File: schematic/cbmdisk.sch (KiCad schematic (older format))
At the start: 26 parts, among them IC1 74HC4050, IC2 ATMEGA1284-P, K1 CONN_3, P1 CONN_2, P2 CONN_12, P3 CONN_12, P4 CONN_5X2, P5 CONN_9, P6 CONN_4, P7 CONN_6, SW1 SW_PUSH, SW2 SWITCH_INV, U1 LM1085, U2 7805, X1 20 MHz

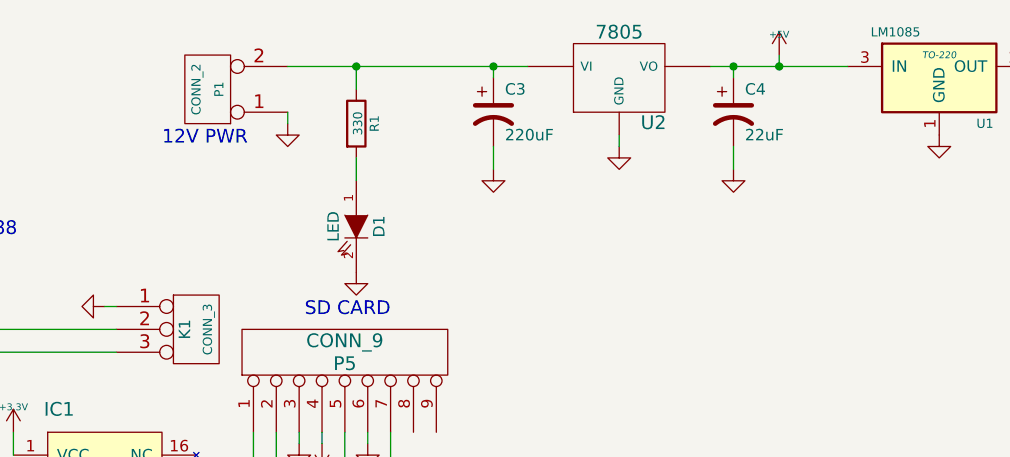
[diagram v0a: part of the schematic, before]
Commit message: remove 5V regulator (use 5V switching power supply)
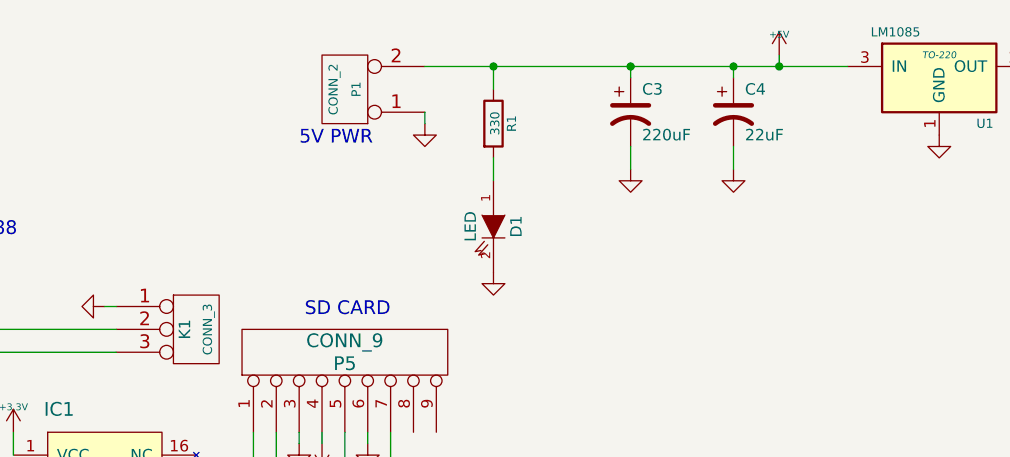
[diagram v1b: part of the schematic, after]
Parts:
- removed U2: 7805, ~, symbol 7805
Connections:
- wire segments 141 -> 139
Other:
- note added: "5V PWR"
- note removed: "12V PWR"
- moved on the sheet: C3, D1, P1, R1
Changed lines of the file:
@@
-$EndComp
-$Comp
-L 7805 U2
-U 1 1 55AB66E8
-P 8400 750
-F 0 "U2" H 8550 554 60  0000 C CNN
-F 1 "7805" H 8400 950 60  0000 C CNN
-F 2 "~" H 8400 750 60  0000 C CNN
-F 3 "~" H 8400 750 60  0000 C CNN
-	1    8400 750
-	1    0    0    -1
 $EndComp
 $Comp
 L CONN_2 P1
 U 1 1 55AB6701
-P 6600 800
-F 0 "P1" V 6550 800 40  0000 C CNN
-F 1 "CONN_2" V 6650 800 40  0000 C CNN
-F 2 "~" H 6600 800 60  0000 C CNN
-F 3 "~" H 6600 800 60  0000 C CNN
-	1    6600 800
+P 7200 800
+F 0 "P1" V 7150 800 40  0000 C CNN
+F 1 "CONN_2" V 7250 800 40  0000 C CNN
+F 2 "~" H 7200 800 60  0000 C CNN
+F 3 "~" H 7200 800 60  0000 C CNN
+	1    7200 800
 	-1   0    0    1
 $EndComp
@@
 L GND #PWR5
 U 1 1 55AB671A
-P 6950 950
-F 0 "#PWR5" H 6950 950 30  0001 C CNN
-F 1 "GND" H 6950 880 30  0001 C CNN
-F 2 "" H 6950 950 60  0000 C CNN
-F 3 "" H 6950 950 60  0000 C CNN
-	1    6950 950
-	1    0    0    -1
-$EndComp
-Text Notes 6400 1050 0    60   ~ 0
-12V PWR
+P 7550 950
+F 0 "#PWR5" H 7550 950 30  0001 C CNN
+F 1 "GND" H 7550 880 30  0001 C CNN
+F 2 "" H 7550 950 60  0000 C CNN
+F 3 "" H 7550 950 60  0000 C CNN
+	1    7550 950
+	1    0    0    -1
+$EndComp
+Text Notes 7000 1050 0    60   ~ 0
+5V PWR
 $Comp
 L CP1 C3
 U 1 1 55AB68A1
-P 7850 900
-F 0 "C3" H 7900 1000 50  0000 L CNN
-F 1 "220uF" H 7900 800 50  0000 L CNN
-F 2 "~" H 7850 900 60  0000 C CNN
-F 3 "~" H 7850 900 60  0000 C CNN
-	1    7850 900
+P 8450 900
+F 0 "C3" H 8500 1000 50  0000 L CNN
+F 1 "220uF" H 8500 800 50  0000 L CNN
+F 2 "~" H 8450 900 60  0000 C CNN
+F 3 "~" H 8450 900 60  0000 C CNN
+	1    8450 900
 	1    0    0    -1
 $EndComp
@@
 L GND #PWR10
 U 1 1 55AB68B0
-P 7850 1150
-F 0 "#PWR10" H 7850 1150 30  0001 C CNN
-F 1 "GND" H 7850 1080 30  0001 C CNN
-F 2 "" H 7850 1150 60  0000 C CNN
-F 3 "" H 7850 1150 60  0000 C CNN
-	1    7850 1150
+P 8450 1150
+F 0 "#PWR10" H 8450 1150 30  0001 C CNN
+F 1 "GND" H 8450 1080 30  0001 C CNN
+F 2 "" H 8450 1150 60  0000 C CNN
+F 3 "" H 8450 1150 60  0000 C CNN
+	1    8450 1150
 	1    0    0    -1
 $EndComp
@@
 $EndComp
 $Comp
-L GND #PWR8
-U 1 1 55AB6C63
-P 8400 1050
-F 0 "#PWR8" H 8400 1050 30  0001 C CNN
-F 1 "GND" H 8400 980 30  0001 C CNN
-F 2 "" H 8400 1050 60  0000 C CNN
-F 3 "" H 8400 1050 60  0000 C CNN
-	1    8400 1050
-	1    0    0    -1
-$EndComp
-$Comp
 L LED D1
 U 1 1 55AB6CED
-P 7250 1400
-F 0 "D1" H 7250 1500 50  0000 C CNN
-F 1 "LED" H 7250 1300 50  0000 C CNN
-F 2 "~" H 7250 1400 60  0000 C CNN
-F 3 "~" H 7250 1400 60  0000 C CNN
-	1    7250 1400
+P 7850 1400
+F 0 "D1" H 7850 1500 50  0000 C CNN
+F 1 "LED" H 7850 1300 50  0000 C CNN
+F 2 "~" H 7850 1400 60  0000 C CNN
+F 3 "~" H 7850 1400 60  0000 C CNN
+	1    7850 1400
 	0    1    1    0
 $EndComp
@@
 L R R1
 U 1 1 55AB6CFC
-P 7250 950
-F 0 "R1" V 7330 950 40  0000 C CNN
-F 1 "330" V 7257 951 40  0000 C CNN
-F 2 "~" V 7180 950 30  0000 C CNN
-F 3 "~" H 7250 950 30  0000 C CNN
-	1    7250 950
+P 7850 950
+F 0 "R1" V 7930 950 40  0000 C CNN
+F 1 "330" V 7857 951 40  0000 C CNN
+F 2 "~" V 7780 950 30  0000 C CNN
+F 3 "~" H 7850 950 30  0000 C CNN
+	1    7850 950
 	1    0    0    -1
 $EndComp
@@
 L GND #PWR15
 U 1 1 55AB6D15
-P 7250 1600
-F 0 "#PWR15" H 7250 1600 30  0001 C CNN
-F 1 "GND" H 7250 1530 30  0001 C CNN
-F 2 "" H 7250 1600 60  0000 C CNN
-F 3 "" H 7250 1600 60  0000 C CNN
-	1    7250 1600
+P 7850 1600
+F 0 "#PWR15" H 7850 1600 30  0001 C CNN
+F 1 "GND" H 7850 1530 30  0001 C CNN
+F 2 "" H 7850 1600 60  0000 C CNN
+F 3 "" H 7850 1600 60  0000 C CNN
+	1    7850 1600
 	1    0    0    -1
 $EndComp
@@
 	5700 4600 5750 4600
 Wire Wire Line
-	6950 950  6950 900
-Wire Wire Line
-	6950 700  8000 700
-Wire Wire Line
-	7850 1050 7850 1150
+	7550 950  7550 900
+Wire Wire Line
+	8450 1050 8450 1150
 Wire Wire Line
 	8900 1050 8900 1150
-Wire Wire Line
-	8800 700  9400 700
-Wire Wire Line
-	8400 1050 8400 1000
 Wire Wire Line
 	3850 4500 3650 4500
@@
 RESET
 Wire Wire Line
-	7250 700  7250 800
-Connection ~ 7250 700
-Wire Wire Line
-	7250 1100 7250 1200
+	7850 700  7850 800
+Connection ~ 7850 700
+Wire Wire Line
+	7850 1100 7850 1200
 Wire Wire Line
 	8900 700  8900 750
 Connection ~ 8900 700
 Wire Wire Line
-	7850 700  7850 750
-Connection ~ 7850 700
+	8450 700  8450 750
+Connection ~ 8450 700
 Wire Wire Line
 	10350 1050 10350 1100
@@
 Wire Wire Line
 	2050 1200 2050 1250
+Wire Wire Line
+	9400 700  7550 700
 $EndSCHEMATC

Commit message: big cleanup, remove network parts
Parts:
- removed P4: CONN_5X2, ~, symbol CONN_5X2
- removed P7: CONN_6, ~, symbol CONN_6
- removed SW2: SWITCH_INV, ~, symbol SWITCH_INV
- added J?: CONN_02X04, symbol CONN_02X04
- D1, D2: symbol LED -> LED-RESCUE-cbmdisk
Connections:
- net labels removed: CLKOUT, CS, ETH_INT, IEC_ATN, IEC_CLK, IEC_DATA, IEC_RESET, IEC_SRQ, SI, SO, VCC, bRESET
- wire segments 139 -> 106
- no-connect marks 0 -> 13
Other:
- note added: "DEBUG"
- note removed: "ETH Module"
- note removed: "IEC PORT"
- note removed: "IEEE488 / IEC"
- moved on the sheet: C2, C3, C4, D1, P1, P5, R1, U1

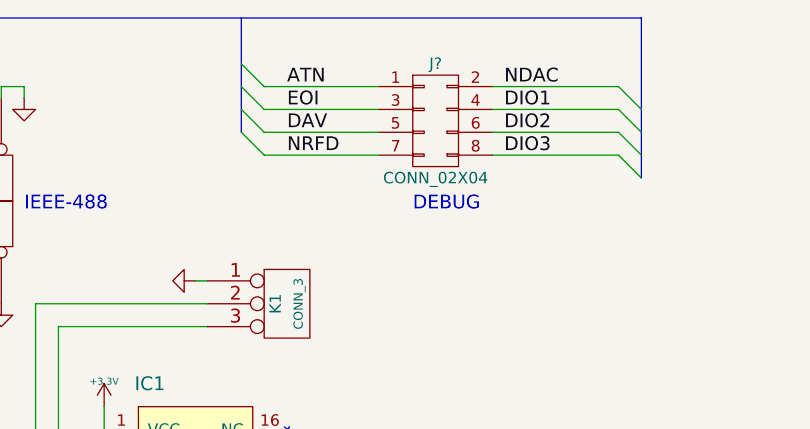
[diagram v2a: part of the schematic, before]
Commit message: update schematic
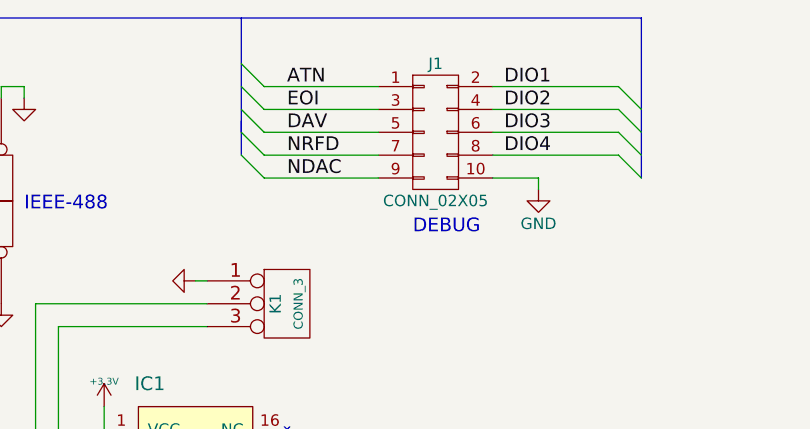
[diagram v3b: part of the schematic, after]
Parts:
- removed J?: CONN_02X04, symbol CONN_02X04
- added J1: CONN_02X05, symbol CONN_02X05
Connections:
- net ATN: now also J1.1 (P1)
- net DAV: now also J1.5 (P5)
- net DIO1: now also J1.2 (P2)
- net DIO2: now also J1.4 (P4)
- net DIO3: now also J1.6 (P6)
- net DIO4: now also J1.8 (P8)
- net EOI: now also J1.3 (P3)
- net GND: now also J1.10 (P10)
- net NDAC: now also J1.9 (P9)
- net NRFD: now also J1.7 (P7)
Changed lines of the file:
@@
 $EndComp
 $Comp
-L GND #PWR24
+L GND #PWR15
 U 1 1 546E9A2F
 P 650 1900
-F 0 "#PWR24" H 650 1900 30  0001 C CNN
+F 0 "#PWR15" H 650 1900 30  0001 C CNN
 F 1 "GND" H 650 1830 30  0001 C CNN
 F 2 "" H 650 1900 60  0000 C CNN
@@
 $EndComp
 $Comp
-L GND #PWR29
+L GND #PWR17
 U 1 1 546E9A3E
 P 650 2500
-F 0 "#PWR29" H 650 2500 30  0001 C CNN
+F 0 "#PWR17" H 650 2500 30  0001 C CNN
 F 1 "GND" H 650 2430 30  0001 C CNN
 F 2 "" H 650 2500 60  0000 C CNN
@@
 $EndComp
 $Comp
-L GND #PWR40
+L GND #PWR28
 U 1 1 5470B949
 P 2650 5300
-F 0 "#PWR40" H 2650 5300 30  0001 C CNN
+F 0 "#PWR28" H 2650 5300 30  0001 C CNN
 F 1 "GND" H 2650 5230 30  0001 C CNN
 F 2 "" H 2650 5300 60  0000 C CNN
@@
 $EndComp
 $Comp
-L GND #PWR39
+L GND #PWR27
 U 1 1 5470B958
 P 2450 5300
-F 0 "#PWR39" H 2450 5300 30  0001 C CNN
+F 0 "#PWR27" H 2450 5300 30  0001 C CNN
 F 1 "GND" H 2450 5230 30  0001 C CNN
 F 2 "" H 2450 5300 60  0000 C CNN
@@
 $EndComp
 $Comp
-L GND #PWR4
+L GND #PWR2
 U 1 1 5470F400
 P 5400 950
-F 0 "#PWR4" H 5400 950 30  0001 C CNN
+F 0 "#PWR2" H 5400 950 30  0001 C CNN
 F 1 "GND" H 5400 880 30  0001 C CNN
 F 2 "" H 5400 950 60  0000 C CNN
@@
 $EndComp
 $Comp
-L GND #PWR17
+L GND #PWR8
 U 1 1 5470F40F
 P 4700 1850
-F 0 "#PWR17" H 4700 1850 30  0001 C CNN
+F 0 "#PWR8" H 4700 1850 30  0001 C CNN
 F 1 "GND" H 4700 1780 30  0001 C CNN
 F 2 "" H 4700 1850 60  0000 C CNN
@@
 $EndComp
 $Comp
-L GND #PWR18
+L GND #PWR9
 U 1 1 5470F41E
 P 4800 1850
-F 0 "#PWR18" H 4800 1850 30  0001 C CNN
+F 0 "#PWR9" H 4800 1850 30  0001 C CNN
 F 1 "GND" H 4800 1780 30  0001 C CNN
 F 2 "" H 4800 1850 60  0000 C CNN
@@
 $EndComp
 $Comp
-L GND #PWR19
+L GND #PWR10
 U 1 1 5470F42D
 P 4900 1850
-F 0 "#PWR19" H 4900 1850 30  0001 C CNN
+F 0 "#PWR10" H 4900 1850 30  0001 C CNN
 F 1 "GND" H 4900 1780 30  0001 C CNN
 F 2 "" H 4900 1850 60  0000 C CNN
@@
 $EndComp
 $Comp
-L GND #PWR20
+L GND #PWR11
 U 1 1 5470F43C
 P 5000 1850
-F 0 "#PWR20" H 5000 1850 30  0001 C CNN
+F 0 "#PWR11" H 5000 1850 30  0001 C CNN
 F 1 "GND" H 5000 1780 30  0001 C CNN
 F 2 "" H 5000 1850 60  0000 C CNN
@@
 $EndComp
 $Comp
-L GND #PWR21
+L GND #PWR12
 U 1 1 5470F44B
 P 5100 1850
-F 0 "#PWR21" H 5100 1850 30  0001 C CNN
+F 0 "#PWR12" H 5100 1850 30  0001 C CNN
 F 1 "GND" H 5100 1780 30  0001 C CNN
 F 2 "" H 5100 1850 60  0000 C CNN
@@
 $EndComp
 $Comp
-L GND #PWR22
+L GND #PWR13
 U 1 1 5470F45A
 P 5200 1850
-F 0 "#PWR22" H 5200 1850 30  0001 C CNN
+F 0 "#PWR13" H 5200 1850 30  0001 C CNN
 F 1 "GND" H 5200 1780 30  0001 C CNN
 F 2 "" H 5200 1850 60  0000 C CNN
@@
 $EndComp
 $Comp
-L GND #PWR23
+L GND #PWR14
 U 1 1 5470F469
 P 5300 1850
-F 0 "#PWR23" H 5300 1850 30  0001 C CNN
+F 0 "#PWR14" H 5300 1850 30  0001 C CNN
 F 1 "GND" H 5300 1780 30  0001 C CNN
 F 2 "" H 5300 1850 60  0000 C CNN
@@
 	4100 2150 4200 2050
 $Comp
-L +5V #PWR3
+L +5V #PWR1
 U 1 1 54723ED9
 P 2450 750
-F 0 "#PWR3" H 2450 840 20  0001 C CNN
+F 0 "#PWR1" H 2450 840 20  0001 C CNN
 F 1 "+5V" H 2450 840 30  0000 C CNN
 F 2 "" H 2450 750 60  0000 C CNN
@@
 $EndComp
 $Comp
-L +3.3V #PWR25
+L +3.3V #PWR16
 U 1 1 5472404F
 P 5750 2300
-F 0 "#PWR25" H 5750 2260 30  0001 C CNN
+F 0 "#PWR16" H 5750 2260 30  0001 C CNN
 F 1 "+3.3V" H 5750 2410 30  0000 C CNN
 F 2 "" H 5750 2300 60  0000 C CNN
@@
 SD CARD
 $Comp
-L GND #PWR26
+L GND #PWR19
 U 1 1 55A40A08
 P 7350 3100
-F 0 "#PWR26" H 7350 3100 30  0001 C CNN
+F 0 "#PWR19" H 7350 3100 30  0001 C CNN
 F 1 "GND" H 7350 3030 30  0001 C CNN
 F 2 "" H 7350 3100 60  0000 C CNN
@@
 $EndComp
 $Comp
-L +3.3V #PWR27
+L +3.3V #PWR20
 U 1 1 55A40A5F
 P 7350 3200
-F 0 "#PWR27" H 7350 3160 30  0001 C CNN
+F 0 "#PWR20" H 7350 3160 30  0001 C CNN
 F 1 "+3.3V" H 7350 3310 30  0000 C CNN
 F 2 "" H 7350 3200 60  0000 C CNN
@@
 $EndComp
 $Comp
-L GND #PWR28
+L GND #PWR21
 U 1 1 55A40B02
 P 7400 3400
-F 0 "#PWR28" H 7400 3400 30  0001 C CNN
+F 0 "#PWR21" H 7400 3400 30  0001 C CNN
 F 1 "GND" H 7400 3330 30  0001 C CNN
 F 2 "" H 7400 3400 60  0000 C CNN
@@
 $EndComp
 $Comp
-L +5V #PWR6
+L +5V #PWR3
 U 1 1 55A6F1C2
 P 1400 1000
-F 0 "#PWR6" H 1400 1090 20  0001 C CNN
+F 0 "#PWR3" H 1400 1090 20  0001 C CNN
 F 1 "+5V" H 1400 1090 30  0000 C CNN
 F 2 "" H 1400 1000 60  0000 C CNN
@@
 $EndComp
 $Comp
-L GND #PWR14
+L GND #PWR6
 U 1 1 55A6F249
 P 750 1600
-F 0 "#PWR14" H 750 1600 30  0001 C CNN
+F 0 "#PWR6" H 750 1600 30  0001 C CNN
 F 1 "GND" H 750 1530 30  0001 C CNN
 F 2 "" H 750 1600 60  0000 C CNN
@@
 READONLY
 $Comp
-L GND #PWR30
+L GND #PWR18
 U 1 1 55A6F5B4
 P 5700 2600
-F 0 "#PWR30" H 5700 2600 30  0001 C CNN
+F 0 "#PWR18" H 5700 2600 30  0001 C CNN
 F 1 "GND" H 5700 2530 30  0001 C CNN
 F 2 "" H 5700 2600 60  0000 C CNN
@@
 $EndComp
 $Comp
-L GND #PWR35
+L GND #PWR22
 U 1 1 55A6FF77
 P 5200 4100
-F 0 "#PWR35" H 5200 4100 30  0001 C CNN
+F 0 "#PWR22" H 5200 4100 30  0001 C CNN
 F 1 "GND" H 5200 4030 30  0001 C CNN
 F 2 "" H 5200 4100 60  0000 C CNN
@@
 $EndComp
 $Comp
-L GND #PWR7
+L GND #PWR30
 U 1 1 55A7740F
 P 9750 5550
-F 0 "#PWR7" H 9750 5550 30  0001 C CNN
+F 0 "#PWR30" H 9750 5550 30  0001 C CNN
 F 1 "GND" H 9750 5480 30  0001 C CNN
 F 2 "" H 9750 5550 60  0000 C CNN
@@
 $EndComp
 $Comp
-L +3.3V #PWR2
+L +3.3V #PWR26
 U 1 1 55A81B2B
 P 10550 5200
-F 0 "#PWR2" H 10550 5160 30  0001 C CNN
+F 0 "#PWR26" H 10550 5160 30  0001 C CNN
 F 1 "+3.3V" H 10550 5310 30  0000 C CNN
 F 2 "" H 10550 5200 60  0000 C CNN
@@
 $EndComp
 $Comp
-L GND #PWR9
+L GND #PWR31
 U 1 1 55A81B53
 P 10300 5650
-F 0 "#PWR9" H 10300 5650 30  0001 C CNN
+F 0 "#PWR31" H 10300 5650 30  0001 C CNN
 F 1 "GND" H 10300 5580 30  0001 C CNN
 F 2 "" H 10300 5650 60  0000 C CNN
@@
 $EndComp
 $Comp
-L GND #PWR36
+L GND #PWR23
 U 1 1 55AB6482
 P 5700 4500
-F 0 "#PWR36" H 5700 4500 30  0001 C CNN
+F 0 "#PWR23" H 5700 4500 30  0001 C CNN
 F 1 "GND" H 5700 4430 30  0001 C CNN
 F 2 "" H 5700 4500 60  0000 C CNN
@@
 $EndComp
 $Comp
-L +5V #PWR37
+L +5V #PWR24
 U 1 1 55AB6505
 P 5700 4600
-F 0 "#PWR37" H 5700 4690 20  0001 C CNN
+F 0 "#PWR24" H 5700 4690 20  0001 C CNN
 F 1 "+5V" H 5700 4690 30  0000 C CNN
 F 2 "" H 5700 4600 60  0000 C CNN
@@
 $EndComp
 $Comp
-L GND #PWR5
+L GND #PWR29
 U 1 1 55AB671A
 P 7500 5500
-F 0 "#PWR5" H 7500 5500 30  0001 C CNN
+F 0 "#PWR29" H 7500 5500 30  0001 C CNN
 F 1 "GND" H 7500 5430 30  0001 C CNN
 F 2 "" H 7500 5500 60  0000 C CNN
@@
 $EndComp
 $Comp
-L GND #PWR10
+L GND #PWR32
 U 1 1 55AB68B0
 P 8400 5700
-F 0 "#PWR10" H 8400 5700 30  0001 C CNN
+F 0 "#PWR32" H 8400 5700 30  0001 C CNN
 F 1 "GND" H 8400 5630 30  0001 C CNN
 F 2 "" H 8400 5700 60  0000 C CNN
@@
 $EndComp
 $Comp
-L GND #PWR11
+L GND #PWR33
 U 1 1 55AB695C
 P 8850 5700
-F 0 "#PWR11" H 8850 5700 30  0001 C CNN
+F 0 "#PWR33" H 8850 5700 30  0001 C CNN
 F 1 "GND" H 8850 5630 30  0001 C CNN
 F 2 "" H 8850 5700 60  0000 C CNN
@@
 $EndComp
 $Comp
-L +5V #PWR1
+L +5V #PWR25
 U 1 1 55AB6AE5
 P 9050 5200
-F 0 "#PWR1" H 9050 5290 20  0001 C CNN
+F 0 "#PWR25" H 9050 5290 20  0001 C CNN
 F 1 "+5V" H 9050 5290 30  0000 C CNN
 F 2 "" H 9050 5200 60  0000 C CNN
@@
 $EndComp
 $Comp
-L GND #PWR15
+L GND #PWR34
 U 1 1 55AB6D15
 P 7800 6150
-F 0 "#PWR15" H 7800 6150 30  0001 C CNN
+F 0 "#PWR34" H 7800 6150 30  0001 C CNN
 F 1 "GND" H 7800 6080 30  0001 C CNN
 F 2 "" H 7800 6150 60  0000 C CNN
@@
 $EndComp
 $Comp
-L GND #PWR16
+L GND #PWR7
 U 1 1 55B167C5
 P 6150 1750
-F 0 "#PWR16" H 6150 1750 30  0001 C CNN
+F 0 "#PWR7" H 6150 1750 30  0001 C CNN
 F 1 "GND" H 6150 1680 30  0001 C CNN
 F 2 "" H 6150 1750 60  0000 C CNN
@@
 	2050 850  2050 900
 $Comp
-L GND #PWR?
+L GND #PWR4
 U 1 1 55CDB00D
 P 2050 1250
-F 0 "#PWR?" H 2050 1000 50  0001 C CNN
+F 0 "#PWR4" H 2050 1000 50  0001 C CNN
 F 1 "GND" H 2050 1100 50  0000 C CNN
 F 2 "" H 2050 1250 60  0000 C CNN
@@
 NoConn ~ 3650 4000
 NoConn ~ 3650 2700
-$Comp
-L CONN_02X04 J?
-U 1 1 5D04CE56
-P 7200 1050
-F 0 "J?" H 7200 1300 50  0000 C CNN
-F 1 "CONN_02X04" H 7200 800 50  0000 C CNN
-F 2 "" H 7200 -150 50  0001 C CNN
-F 3 "" H 7200 -150 50  0001 C CNN
-	1    7200 1050
-	1    0    0    -1
-$EndComp
 Wire Wire Line
 	7400 3550 7400 3500
@@
 Text Label 6550 1200 0    60   ~ 0
 NRFD
+Entry Wire Line
+	8000 1200 8100 1300
+Entry Wire Line
+	8000 1100 8100 1200
+Entry Wire Line
+	8000 1000 8100 1100
+Entry Wire Line
+	8000 900  8100 1000
+Wire Wire Line
+	8000 900  7450 900
+Wire Wire Line
+	8000 1000 7450 1000
+Wire Wire Line
+	8000 1100 7450 1100
+Wire Wire Line
+	8000 1200 7450 1200
+Text Label 6550 1300 0    60   ~ 0
+NDAC
+Text Label 7500 900  0    60   ~ 0
+DIO1
+Text Label 7500 1000 0    60   ~ 0
+DIO2
+Text Label 7500 1100 0    60   ~ 0
+DIO3
+Text Notes 7100 1550 0    60   ~ 0
+DEBUG
+$Comp
+L CONN_02X05 J1
+U 1 1 5D05148D
+P 7200 1100
+F 0 "J1" H 7200 1400 50  0000 C CNN
+F 1 "CONN_02X05" H 7200 800 50  0000 C CNN
+F 2 "" H 7200 -100 50  0001 C CNN
+F 3 "" H 7200 -100 50  0001 C CNN
+	1    7200 1100
+	1    0    0    -1
+$EndComp
+Wire Bus Line
+	6350 1050 6350 1200
+Entry Wire Line
+	6350 1200 6450 1300
+Wire Wire Line
+	6450 1300 6950 1300
+Wire Wire Line
+	7450 1300 7650 1300
+Wire Wire Line
+	7650 1300 7650 1350
+$Comp
+L GND #PWR5
+U 1 1 5D0518AE
+P 7650 1350
+F 0 "#PWR5" H 7650 1100 50  0001 C CNN
+F 1 "GND" H 7650 1200 50  0000 C CNN
+F 2 "" H 7650 1350 50  0001 C CNN
+F 3 "" H 7650 1350 50  0001 C CNN
+	1    7650 1350
+	1    0    0    -1
+$EndComp
 Wire Bus Line
 	8100 600  8100 1300
-Entry Wire Line
-	8000 1200 8100 1300
-Entry Wire Line
-	8000 1100 8100 1200
-Entry Wire Line
-	8000 1000 8100 1100
-Entry Wire Line
-	8000 900  8100 1000
-Wire Wire Line
-	8000 900  7450 900
-Wire Wire Line
-	8000 1000 7450 1000
-Wire Wire Line
-	8000 1100 7450 1100
-Wire Wire Line
-	8000 1200 7450 1200
-Text Label 7500 900  0    60   ~ 0
-NDAC
-Text Label 7500 1000 0    60   ~ 0
-DIO1
-Text Label 7500 1100 0    60   ~ 0
-DIO2
 Text Label 7500 1200 0    60   ~ 0
-DIO3
-Text Notes 7100 1450 0    60   ~ 0
-DEBUG
+DIO4
 $EndSCHEMATC
